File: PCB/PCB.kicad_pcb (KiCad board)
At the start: 2 copper layers, 130.8 x 85.1 mm, 49 parts, among them J1 Conn_01x04_Female, J10 Conn_01x08_Female, J11 Conn_01x01_Female, J12 Conn_01x04_Female, J2 Conn_01x28_Female, J3 Conn_01x02_Female, J4 Conn_01x02_Female, J5 Conn_01x02_Female, J6 Conn_01x02_Female, J7 Conn_01x08_Female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

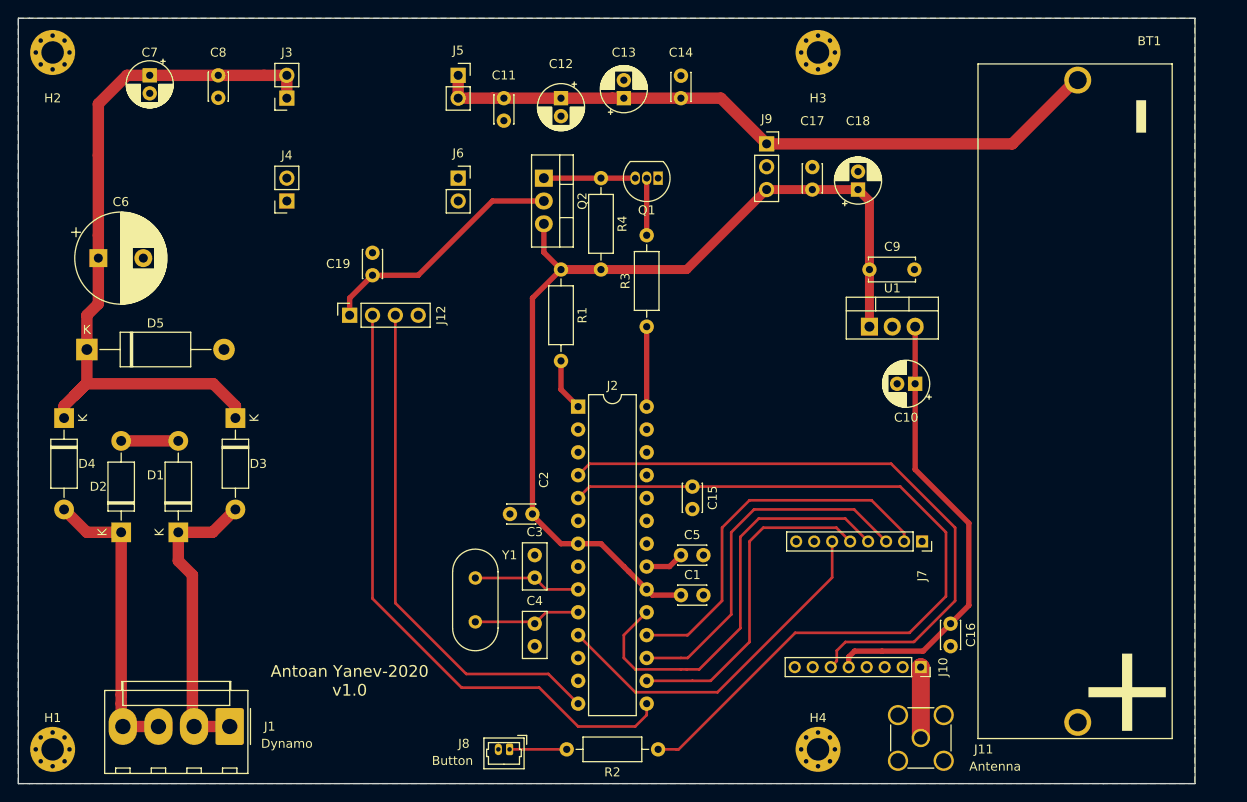
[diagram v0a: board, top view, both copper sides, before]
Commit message: Added UART Header
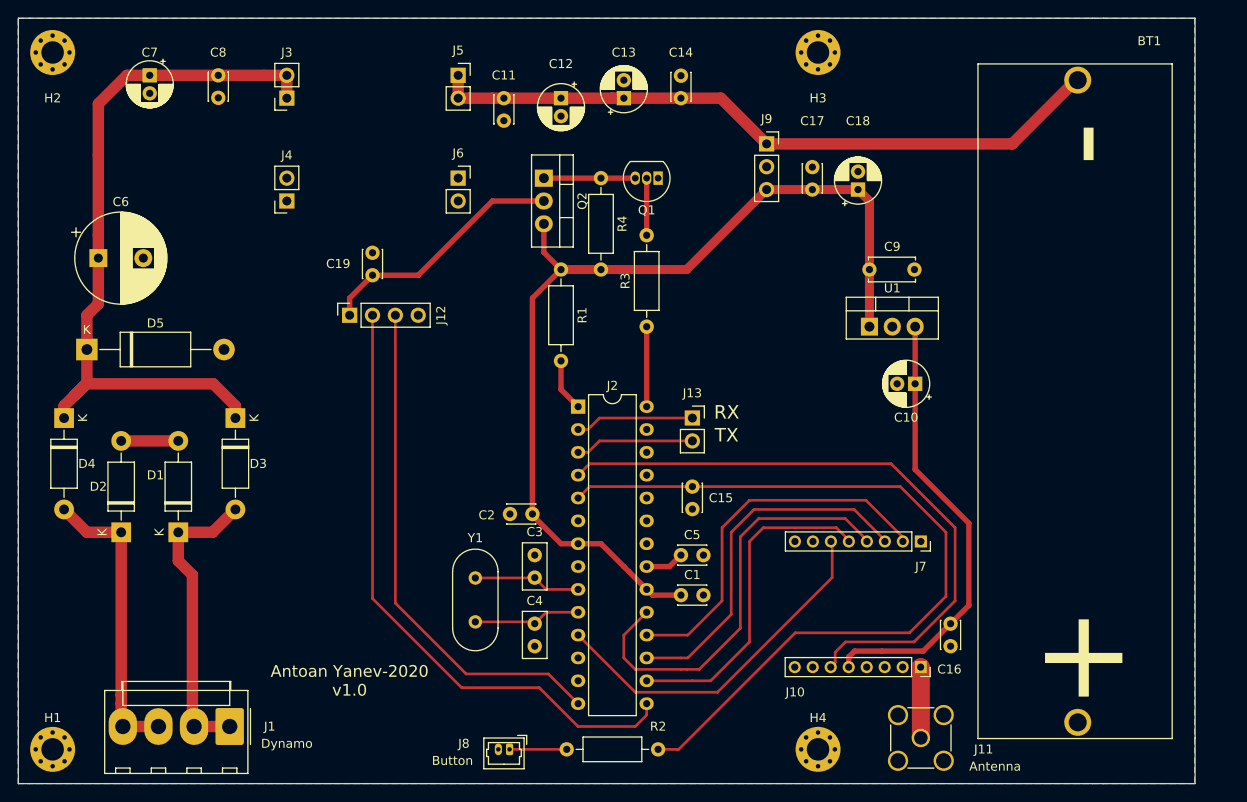
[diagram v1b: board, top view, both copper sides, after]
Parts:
- added J13: Conn_01x02_Female, Connector_PinSocket_2.54mm:PinSocket_1x02_P2.54mm_Vertical, F.Cu at (121.9, 62.2)
- moved J7 0.14 mm to (147.3, 75.9)
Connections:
- J2 pad 2: Net-(J2-Pad2) -> UART_RX
- J2 pad 3: Net-(J2-Pad3) -> UART_TX
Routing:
- net UART_TX: track 0.00 -> 14.1 mm
- net UART_RX: track 0.00 -> 13.2 mm
- net Net-(D2-Pad1): track 36.9 -> 33.0 mm
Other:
- net class Default: clearance 0.2 -> 0.3; trace_width 0.25 -> 0.3
- rule trace_clearance: 0.2 -> 0.3
- board text added: "RX"
- board text added: "TX"

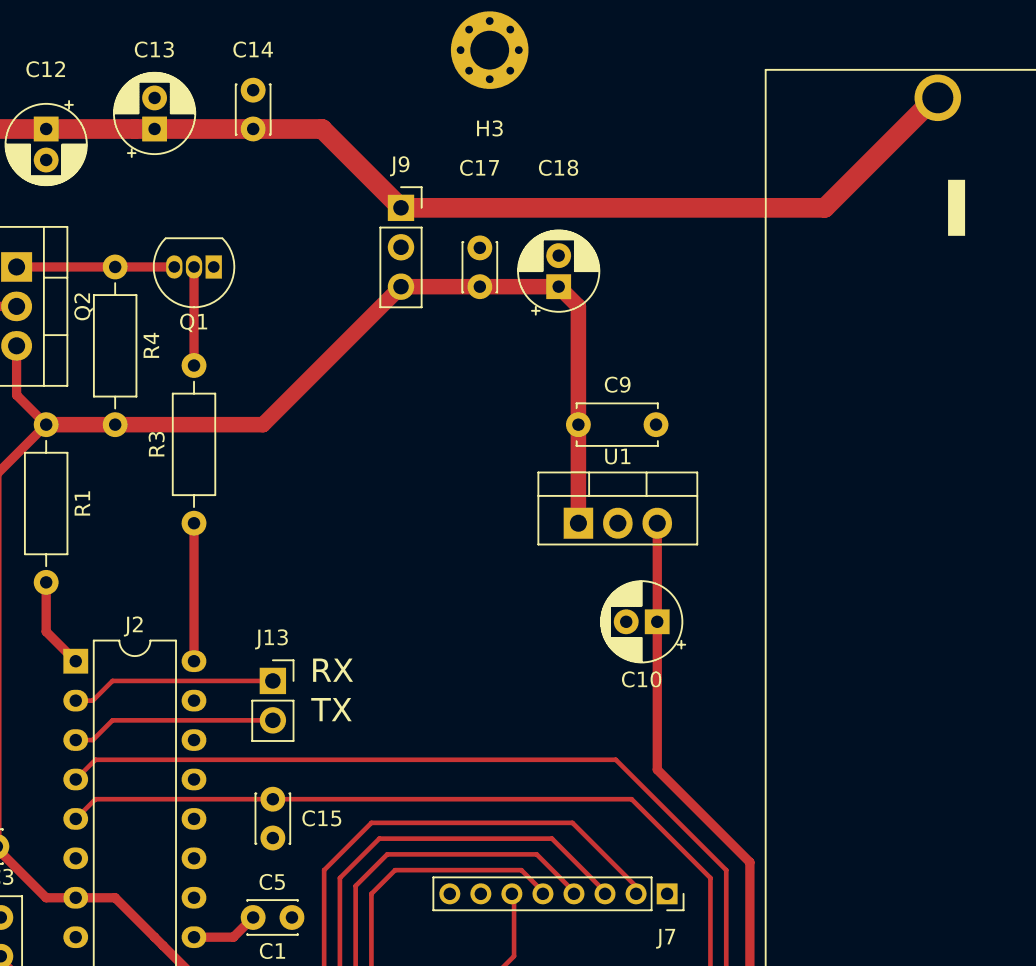
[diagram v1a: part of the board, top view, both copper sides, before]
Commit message: Added batter measuring resistor
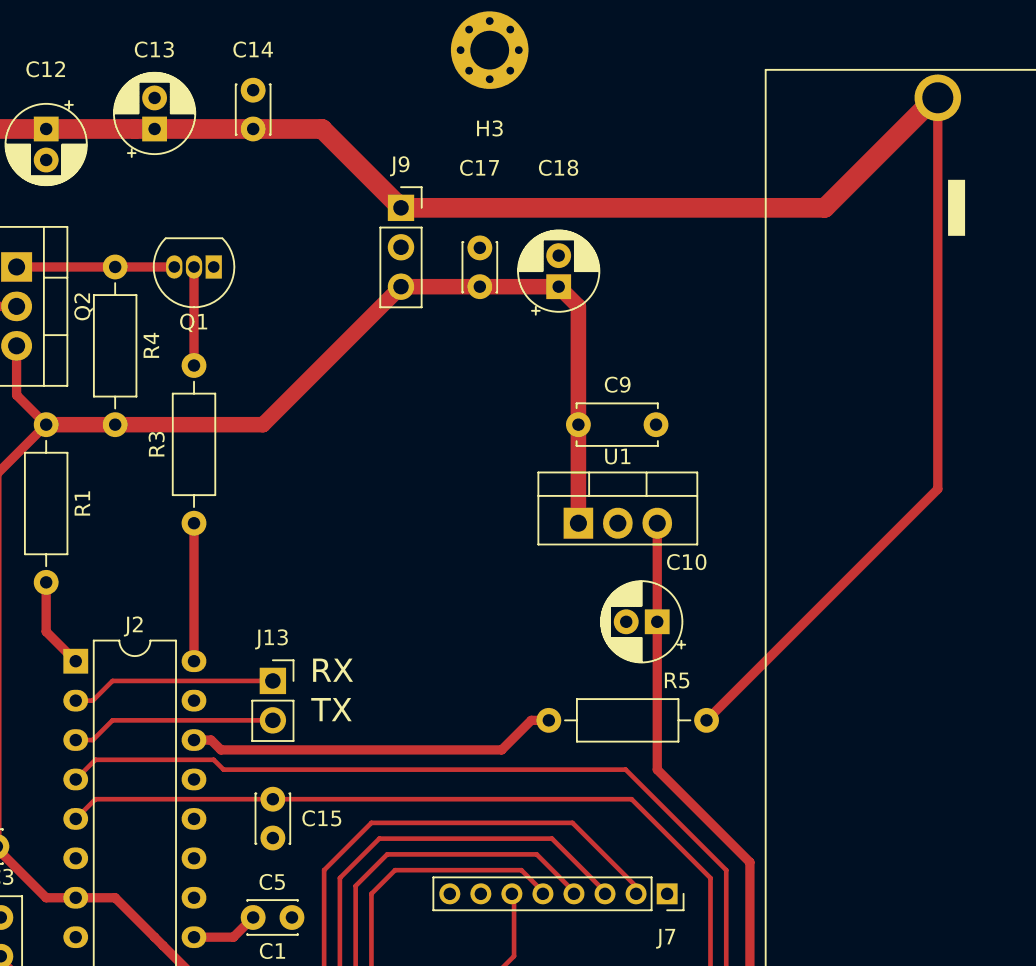
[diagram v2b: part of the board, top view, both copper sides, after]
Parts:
- added R5: 10k, Resistor_THT:R_Axial_DIN0207_L6.3mm_D2.5mm_P10.16mm_Horizontal, F.Cu at (139.7, 64.8)
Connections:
- net Net-(BT1-Pad1) renamed VBAT
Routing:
- net VBAT: track 76.5 -> 122.7 mm
- net Net-(J2-Pad26): track 0.00 -> 23.9 mm
